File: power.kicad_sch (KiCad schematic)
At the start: 20 parts, among them SW1 SW_Push_DPDT, U1 AMS1117-3.3, U3 TPS54302

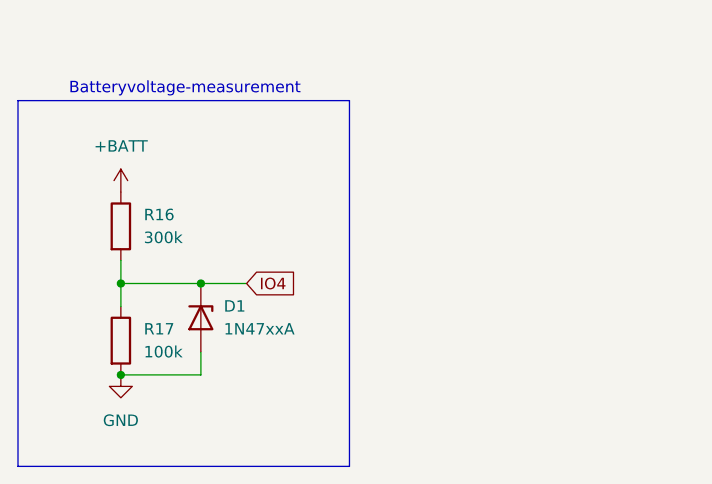
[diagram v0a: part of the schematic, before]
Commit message: simulated IR-constant-current circuit, worked on schematic
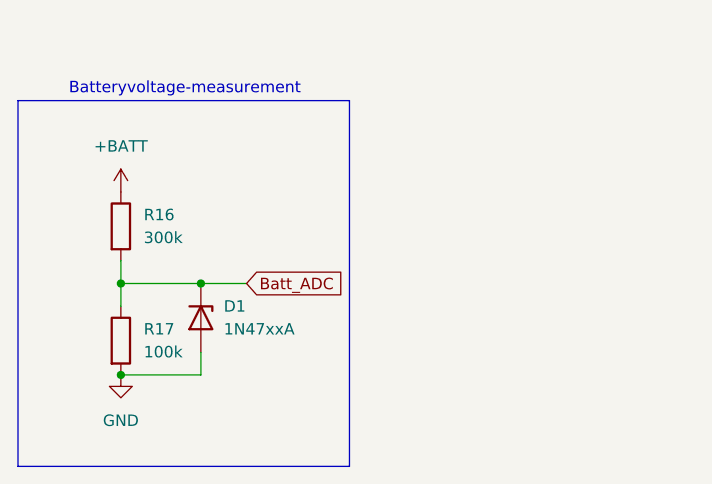
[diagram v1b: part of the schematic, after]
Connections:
- net IO4 renamed Batt_ADC
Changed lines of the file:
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@@
 		)
 	)
-	(global_label "IO4"
+	(global_label "Batt_ADC"
 		(shape input)
 		(at 52.07 96.52 0)
@@
 		)
 		(property "Intersheetrefs" "${INTERSHEET_REFS}"
-			(at 58.2 96.52 0)
+			(at 63.5218 96.52 0)
 			(effects
 				(font

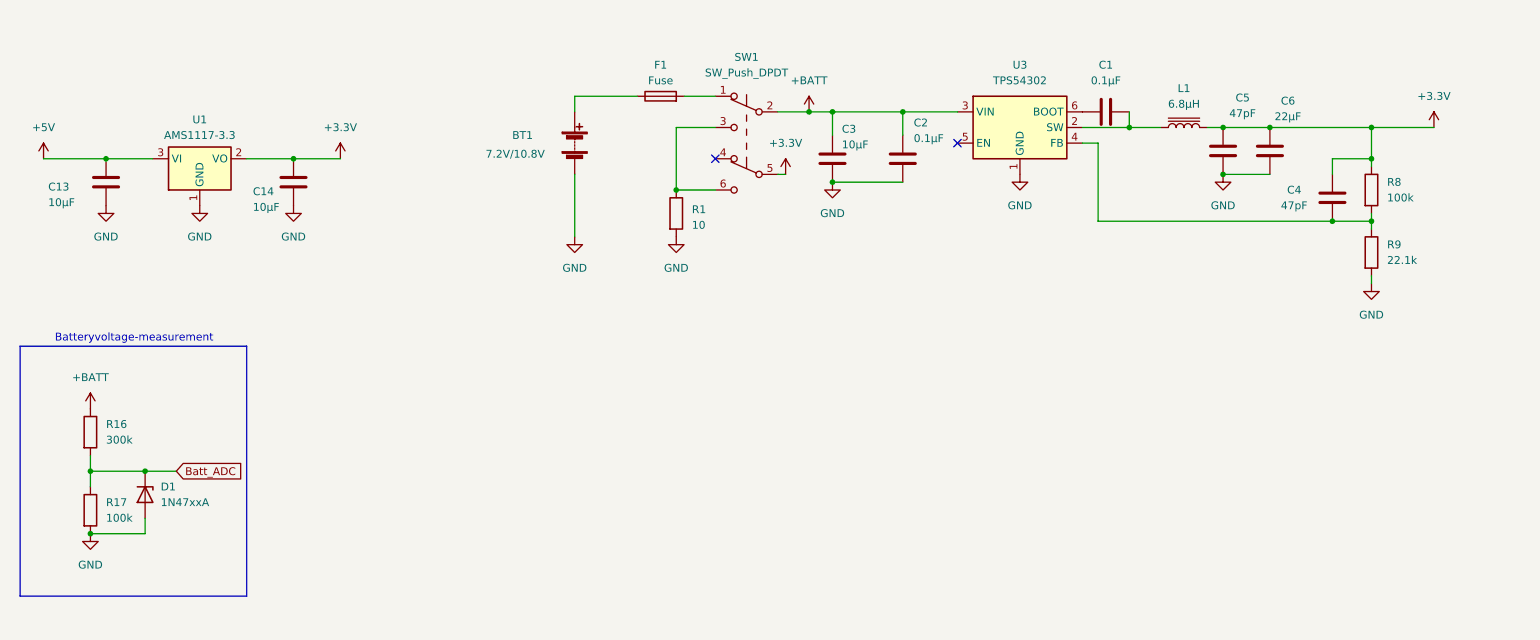
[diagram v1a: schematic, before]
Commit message: prepared for jlcpcb ordering.
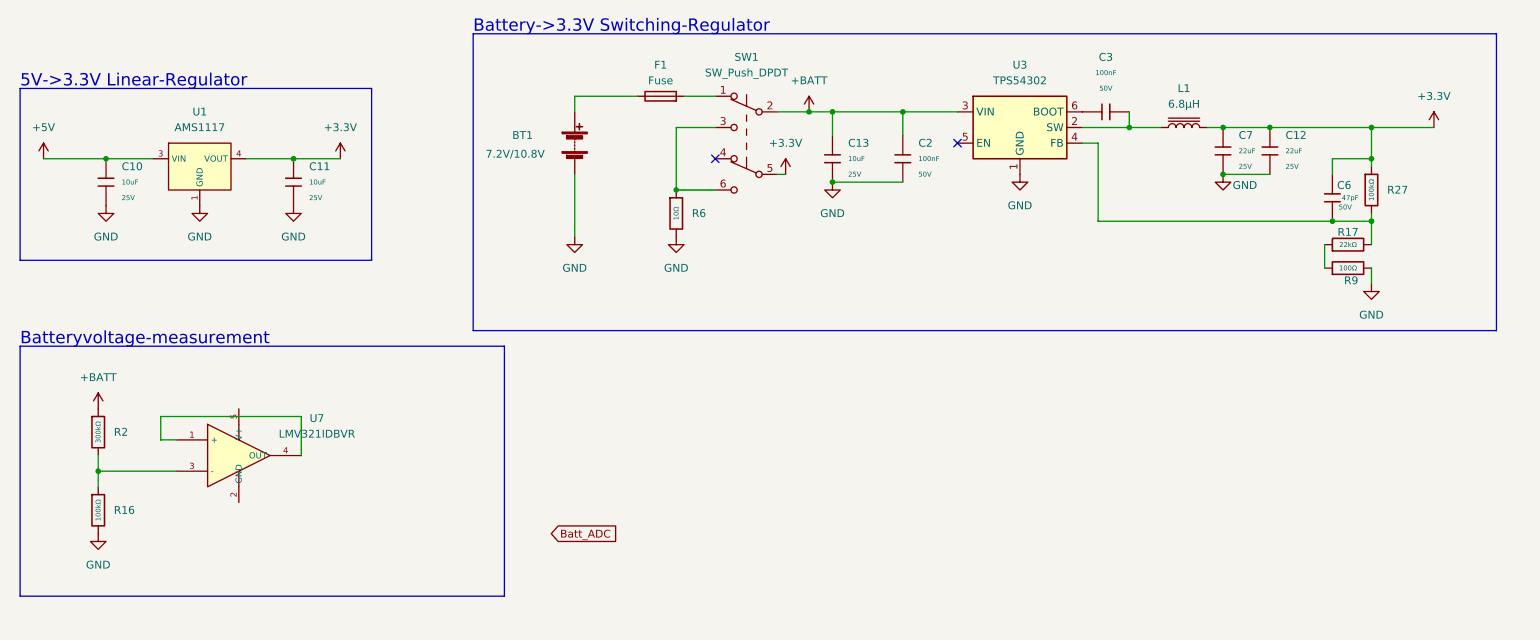
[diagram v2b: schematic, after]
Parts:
- removed C1, C2: 0.1µF, symbol Device:C
- removed C13, C14, C3: 10µF, symbol Device:C
- removed C4, C5: 47pF, symbol Device:C
- removed C6: 22µF, symbol Device:C
- removed D1: 1N47xxA, Diode_THT:D_DO-41_SOD81_P10.16mm_Horizontal, symbol Diode:1N47xxA
- removed R1: 10, symbol Device:R
- removed R16: 300k, symbol Device:R
- removed R17, R8: 100k, symbol Device:R
- removed R9: 22.1k, symbol Device:R
- removed U1: AMS1117-3.3, Package_TO_SOT_SMD:SOT-223-3_TabPin2, symbol Regulator_Linear:AMS1117-3.3
- added C10, C11, C13: 10uF, PCM_JLCPCB:C_0805, symbol PCM_JLCPCB-Capacitors:0805,10uF
- added C12, C7: 22uF, PCM_JLCPCB:C_0805, symbol PCM_JLCPCB-Capacitors:0805,22uF
- added C2, C3: 100nF, PCM_JLCPCB:C_0603, symbol PCM_JLCPCB-Capacitors:0603,100nF
- added C6: 47pF, PCM_JLCPCB:C_0603, symbol PCM_JLCPCB-Capacitors:0603,47pF
- added R16, R27: 100kΩ, PCM_JLCPCB:R_0603, symbol PCM_JLCPCB-Resistors:0603,100kΩ
- added R17: 22kΩ, PCM_JLCPCB:R_0603, symbol PCM_JLCPCB-Resistors:0603,22kΩ
- added R2: 300kΩ, PCM_JLCPCB:R_0603, symbol PCM_JLCPCB-Resistors:0603,300kΩ
- added R6: 10Ω, PCM_JLCPCB:R_0603, symbol PCM_JLCPCB-Resistors:0603,10Ω
- added R9: 100Ω, PCM_JLCPCB:R_0603, symbol PCM_JLCPCB-Resistors:0603,100Ω
- added U1: AMS1117, PCM_JLCPCB:SOT-223-3_L6.5-W3.4-P2.30-LS7.0-BR, symbol PCM_JLCPCB-Power:LDO, 3.3V, 1A
- added U7: LMV321IDBVR, PCM_JLCPCB:SOT-23-5_L3.0-W1.7-P0.95-LS2.8-BR, symbol PCM_JLCPCB-Analog:Op-Amp, LMV321IDBVR
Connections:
- net +3.3V: now also C11.1, C12.1, C6.1, C7.1, R27.1, U1.2 (VOUT), U1.4 (VOUT)
- net +5V: now also C10.1, U1.3 (VIN)
- net +BATT: now also C13.1, C2.1, R2.1
- net GND: now also C10.2, C11.2, C12.2, C13.2, C2.2, C7.2, R16.2, R6.2, R9.2, U1.1 (GND)
- net at U3.4 (FB): now also C6.2, R17.2, R27.2
- net at SW1.3 (C), SW1.6 (C): now also R6.1
- net at L1.1, U3.2 (SW): now also C3.2
- net at U3.6 (BOOT): now also C3.1
- new net: U7.1 (+), U7.4 (OUT)
- new net: R16.1, R2.2, U7.3 (-)
- new net: R17.1, R9.1
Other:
- note added: "5V->3.3V Linear-Regulator"
- note added: "Battery->3.3V Switching-Regulator"

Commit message: checked and fixed schematic, analized it with traceformer.io ai
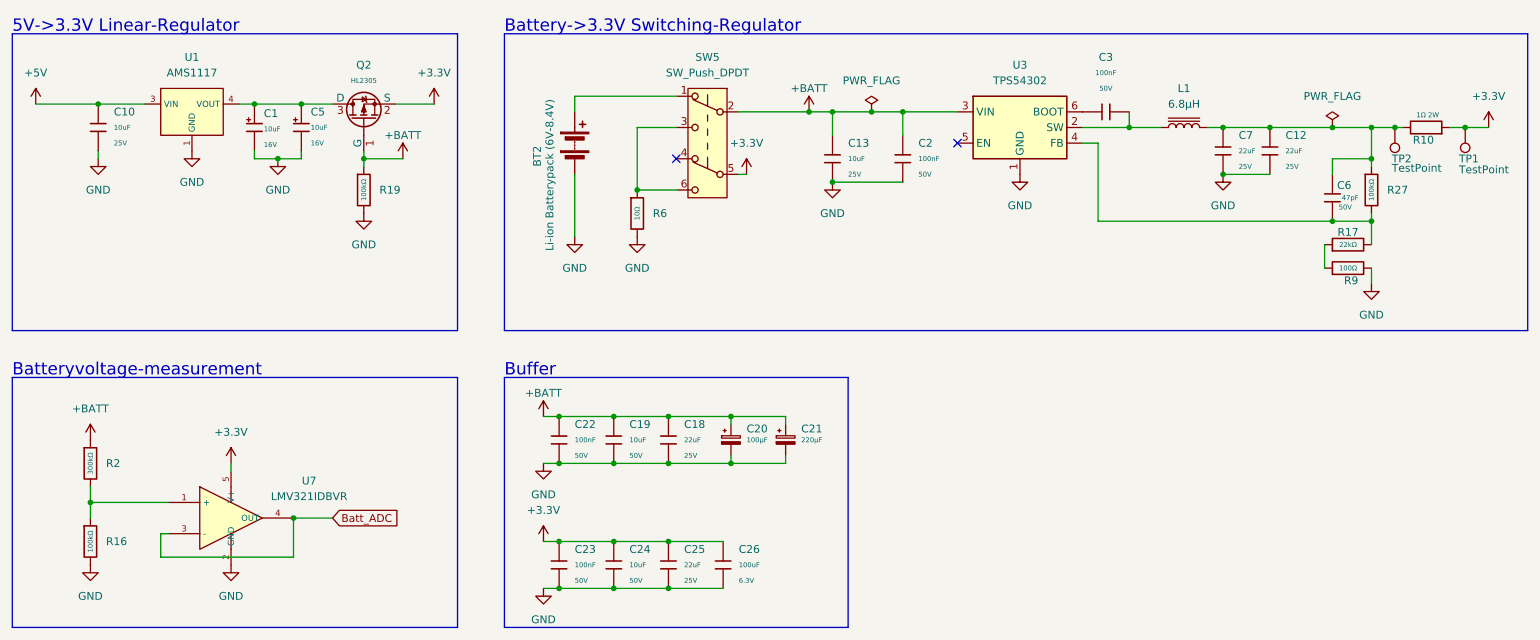
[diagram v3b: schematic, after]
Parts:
- removed BT1: 7.2V/10.8V, symbol Device:Battery
- removed C11: 10uF, PCM_JLCPCB:C_0805, symbol PCM_JLCPCB-Capacitors:0805,10uF
- removed F1: Fuse, symbol Device:Fuse
- removed SW1: SW_Push_DPDT, symbol Switch:SW_Push_DPDT
- added BT2: Li-ion Batterypack (6V-8.4V), Connector_PinHeader_1.00mm:PinHeader_1x02_P1.00mm_Horizontal, symbol Device:Battery
- added C1, C5: 10uF, PCM_JLCPCB:C_CASE-A-3216-18(mm), symbol PCM_JLCPCB-Capacitors:CASE-A-3216-18(mm),10uF
- added C18, C25: 22uF, PCM_JLCPCB:C_1206, symbol PCM_JLCPCB-Capacitors:1206,22uF,(2)
- added C19, C24: 10uF, PCM_JLCPCB:C_1206, symbol PCM_JLCPCB-Capacitors:1206,10uF
- added C20: 100µF, Capacitor_THT:CP_Radial_D5.0mm_P2.50mm, symbol Device:C_Polarized_Small
- added C21: 220µF, Capacitor_THT:CP_Radial_D6.3mm_P2.50mm, symbol Device:C_Polarized_Small
- added C22, C23: 100nF, PCM_JLCPCB:C_1206, symbol PCM_JLCPCB-Capacitors:1206,100nF
- added C26: 100uF, PCM_JLCPCB:C_1206, symbol PCM_JLCPCB-Capacitors:1206,100uF
- added Q2: HL2305, PCM_JLCPCB:Q_SOT-23, symbol PCM_JLCPCB-Transistors:PMOS,HL2305
- added R10: 1Ω 2W, Resistor_SMD:R_2512_6332Metric_Pad1.40x3.35mm_HandSolder, symbol Device:R
- added R19: 100kΩ, PCM_JLCPCB:R_0805, symbol PCM_JLCPCB-Resistors:0805,100kΩ
- added SW5: SW_Push_DPDT, nnaf:MHPS2266, symbol Switch:SW_Push_DPDT
- added TP1, TP2: TestPoint, TestPoint:TestPoint_Pad_D3.0mm, symbol Connector:TestPoint
- L1: footprint (none) -> Inductor_SMD:L_Coilcraft_LPS5030
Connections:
- net +3.3V: now also U7.5 (V+), C23.1, C24.1, C25.1, C26.1, Q2.2 (S), R10.2, SW5.5 (B), TP1.1; no longer C12.1, C6.1, C7.1, L1.2, R27.1, U1.2 (VOUT), U1.4 (VOUT)
- net +BATT: now also C18.1, C19.1, C20.1, C21.1, C22.1, Q2.1 (G), R19.1, SW5.2 (B)
- net Batt_ADC: now also U7.3 (-), U7.4 (OUT)
- net GND: now also U7.2 (GND), BT2.2 (-), C1.2, C18.2, C19.2, C20.2, C21.2, C22.2, C23.2, C24.2, C25.2, C26.2, C5.2, R19.2
- net at U7.1 (+): now also R16.1, R2.2; no longer U7.4 (OUT)
- net at R6.1: now also SW5.3 (C), SW5.6 (C)
- new net: C12.1, C6.1, C7.1, L1.2, R10.1, R27.1, TP2.1
- new net: BT2.1 (+), SW5.1 (A)
- new net: C1.1, C5.1, Q2.3 (D), U1.2 (VOUT), U1.4 (VOUT)
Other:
- note added: "Buffer"
- moved on the sheet: C10, R16, R2, R6, U1, U7

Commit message: replaced ir-led constant current circuit
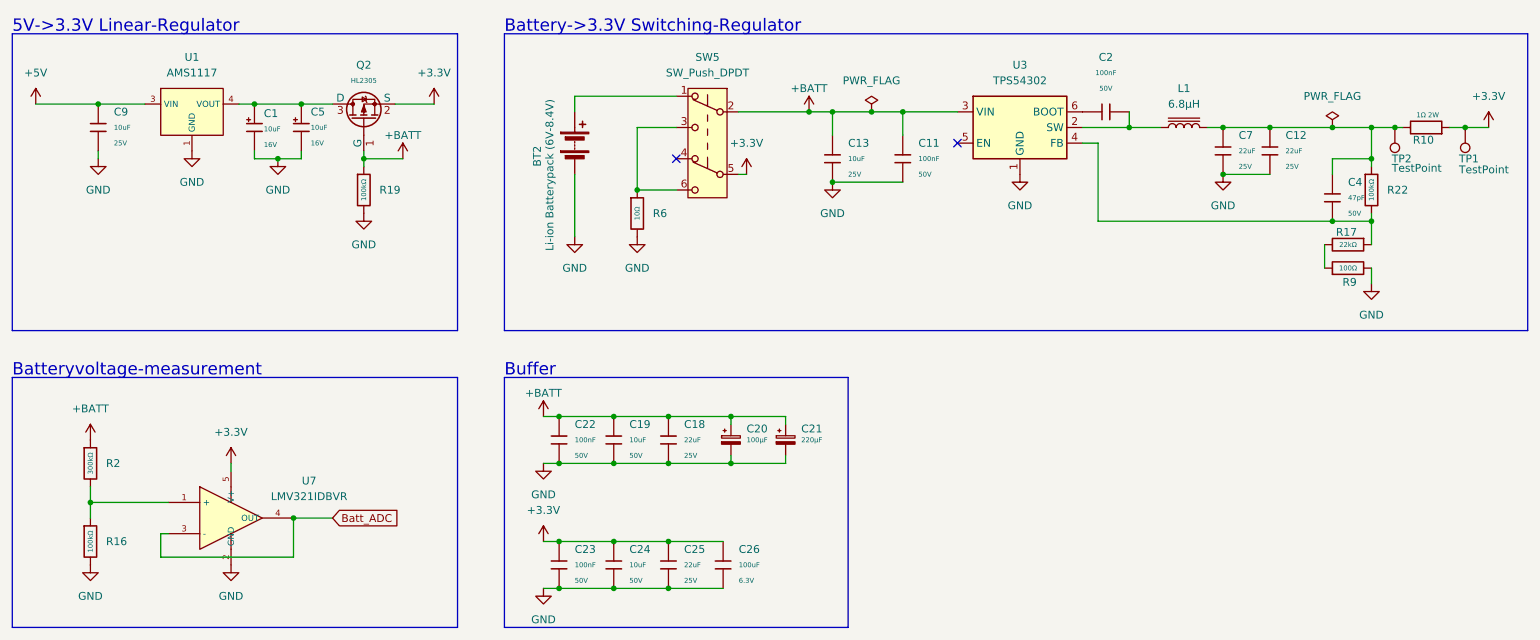
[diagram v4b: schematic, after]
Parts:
- removed C10: 10uF, PCM_JLCPCB:C_0805, symbol PCM_JLCPCB-Capacitors:0805,10uF
- removed C2, C3: 100nF, PCM_JLCPCB:C_0603, symbol PCM_JLCPCB-Capacitors:0603,100nF
- removed C6: 47pF, PCM_JLCPCB:C_0603, symbol PCM_JLCPCB-Capacitors:0603,47pF
- removed R16, R27: 100kΩ, PCM_JLCPCB:R_0603, symbol PCM_JLCPCB-Resistors:0603,100kΩ
- removed R17: 22kΩ, PCM_JLCPCB:R_0603, symbol PCM_JLCPCB-Resistors:0603,22kΩ
- removed R2: 300kΩ, PCM_JLCPCB:R_0603, symbol PCM_JLCPCB-Resistors:0603,300kΩ
- removed R6: 10Ω, PCM_JLCPCB:R_0603, symbol PCM_JLCPCB-Resistors:0603,10Ω
- removed R9: 100Ω, PCM_JLCPCB:R_0603, symbol PCM_JLCPCB-Resistors:0603,100Ω
- added C11, C2: 100nF, PCM_JLCPCB:C_0805, symbol PCM_JLCPCB-Capacitors:0805,100nF,(2)
- added C4: 47pF, PCM_JLCPCB:C_0805, symbol PCM_JLCPCB-Capacitors:0805,47pF
- added C9: 10uF, PCM_JLCPCB:C_0805, symbol PCM_JLCPCB-Capacitors:0805,10uF
- added R16, R22: 100kΩ, PCM_JLCPCB:R_0805, symbol PCM_JLCPCB-Resistors:0805,100kΩ
- added R17: 22kΩ, PCM_JLCPCB:R_0805, symbol PCM_JLCPCB-Resistors:0805,22kΩ
- added R2: 300kΩ, PCM_JLCPCB:R_0805, symbol PCM_JLCPCB-Resistors:0805,300kΩ
- added R6: 10Ω, PCM_JLCPCB:R_0805, symbol PCM_JLCPCB-Resistors:0805,10Ω
- added R9: 100Ω, PCM_JLCPCB:R_0805, symbol PCM_JLCPCB-Resistors:0805,100Ω
- R19: Stock 2411637 -> 3946237
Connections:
- net +5V: now also C9.1
- net +BATT: now also C11.1, R2.1
- net GND: now also C11.2, C9.2, R16.2, R6.2, R9.2
- net at C12.1, C7.1, L1.2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: now also C4.1, R22.1
- net at U7.1 (+): now also R16.1, R2.2
- net at U3.4 (FB): now also C4.2, R17.1, R22.2
- net at SW5.3 (C), SW5.6 (C): now also R6.1
- net at U3.6 (BOOT): now also C2.1
- net at L1.1, U3.2 (SW): now also C2.2
- new net: R17.2, R9.1

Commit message: pcb layout designing
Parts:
- BT2: footprint Connector_PinHeader_1.00mm:PinHeader_1x02_P1.00mm_Horizontal -> Connector_PinHeader_2.54mm:PinHeader_1x02_P2.54mm_Vertical
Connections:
- net at C12.1, C7.1, L1.2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: now also C4.2; no longer C4.1
- net at R17.1, R22.2, U3.4 (FB): now also C4.1; no longer C4.2
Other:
- moved on the sheet: C4
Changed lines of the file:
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@@
 	)
 	(junction
-		(at 240.03 55.88)
-		(diameter 0)
-		(color 0 0 0 0)
-	)
-	(junction
 		(at 222.25 48.26)
 		(diameter 0)
@@
 	)
 	(junction
+		(at 240.03 55.88)
+		(diameter 0)
+		(color 0 0 0 0)
+	)
+	(junction
 		(at 114.3 107.95)
 		(diameter 0)
@@
 	(wire
 		(pts
-			(xy 132.08 115.57) (xy 123.19 115.57)
+			(xy 240.03 55.88) (xy 246.38 55.88)
 		)
 		(stroke
@@
 	(wire
 		(pts
-			(xy 50.8 106.68) (xy 49.53 106.68)
+			(xy 132.08 115.57) (xy 123.19 115.57)
 		)
 		(stroke
@@
 	(wire
 		(pts
-			(xy 82.55 45.72) (xy 82.55 46.99)
+			(xy 50.8 106.68) (xy 49.53 106.68)
 		)
 		(stroke
@@
 	(wire
 		(pts
-			(xy 240.03 40.64) (xy 246.38 40.64)
+			(xy 82.55 45.72) (xy 82.55 46.99)
 		)
 		(stroke
@@
 	(wire
 		(pts
-			(xy 240.03 55.88) (xy 246.38 55.88)
+			(xy 240.03 40.64) (xy 246.38 40.64)
 		)
 		(stroke
@@
 	(symbol
 		(lib_id "PCM_JLCPCB-Capacitors:0805,47pF")
-		(at 240.03 52.07 0)
+		(at 240.03 52.07 180)
 		(unit 1)
 		(exclude_from_sim no)
@@
 					(size 1.27 1.27)
 				)
-				(justify left)
+				(justify right)
 			)
 		)
@@
 					(size 0.8 0.8)
 				)
-				(justify left)
+				(justify right)
 			)
 		)
 		(property "Footprint" "PCM_JLCPCB:C_0805"
-			(at 238.252 52.07 90)
+			(at 241.808 52.07 90)
 			(effects
 				(font
@@
 					(size 0.8 0.8)
 				)
-				(justify left)
+				(justify right)
 			)
 		)
@@
 			)
 		)
-		(property "Footprint" "Connector_PinHeader_1.00mm:PinHeader_1x02_P1.00mm_Horizontal"
+		(property "Footprint" "Connector_PinHeader_2.54mm:PinHeader_1x02_P2.54mm_Vertical"
 			(at 116.84 41.656 90)
 			(effects

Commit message: pcb didn't commit correctly
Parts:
- removed C21: 220µF, Capacitor_THT:CP_Radial_D6.3mm_P2.50mm, symbol Device:C_Polarized_Small
- removed C23: 100nF, PCM_JLCPCB:C_1206, symbol PCM_JLCPCB-Capacitors:1206,100nF
- removed C25: 22uF, PCM_JLCPCB:C_1206, symbol PCM_JLCPCB-Capacitors:1206,22uF,(2)
- added TP7: TestPoint, TestPoint:TestPoint_Pad_D1.5mm, symbol Connector:TestPoint
- L1: footprint Inductor_SMD:L_Coilcraft_LPS5030 -> Inductor_SMD:L_Coilcraft_LPS4018
- TP1: value TestPoint -> 3.3V; footprint TestPoint:TestPoint_Pad_D3.0mm -> TestPoint:TestPoint_Pad_D2.0mm
- TP2: value TestPoint -> total-current; footprint TestPoint:TestPoint_Pad_D3.0mm -> TestPoint:TestPoint_Pad_D1.5mm
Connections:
- net Batt_ADC: now also TP7.1
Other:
- moved on the sheet: C24, C26
